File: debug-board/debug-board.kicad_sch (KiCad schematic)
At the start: 31 parts, among them J1 Conn_01x02_Pin, J13 Conn_01x05_Pin, J14 Conn_01x02_Pin, J16 Conn_01x02_Pin, J17 Conn_01x02_Pin, U1 PIC18F47Q84-I/PT, U2 MAX3051ESA+, U3 AZ1117CH-3.3TRG1, Y2 40MHz

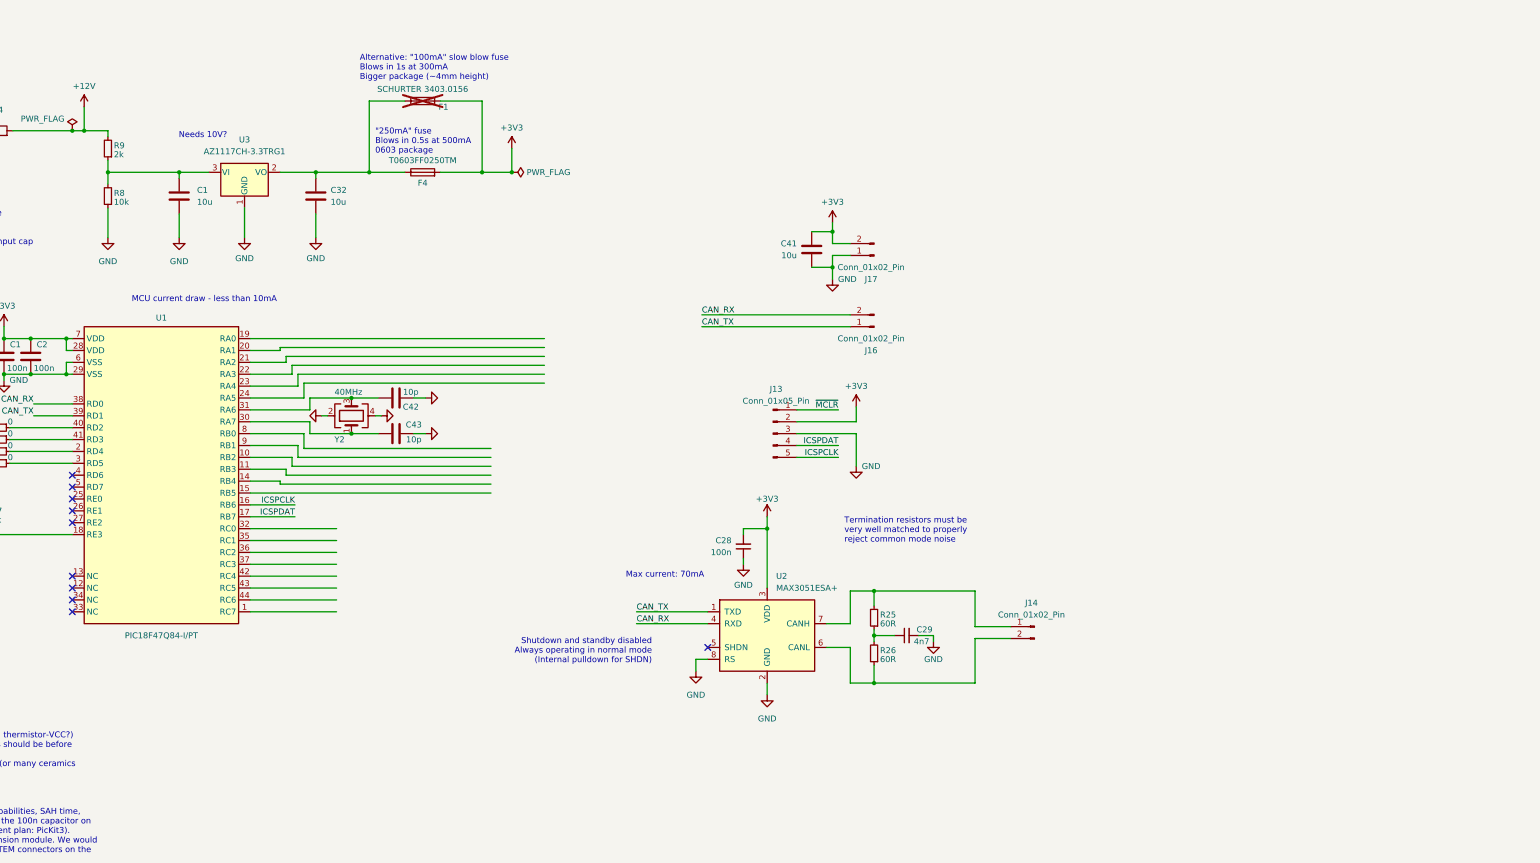
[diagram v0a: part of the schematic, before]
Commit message: Initial design of 12V -> 3V coverter for ADC
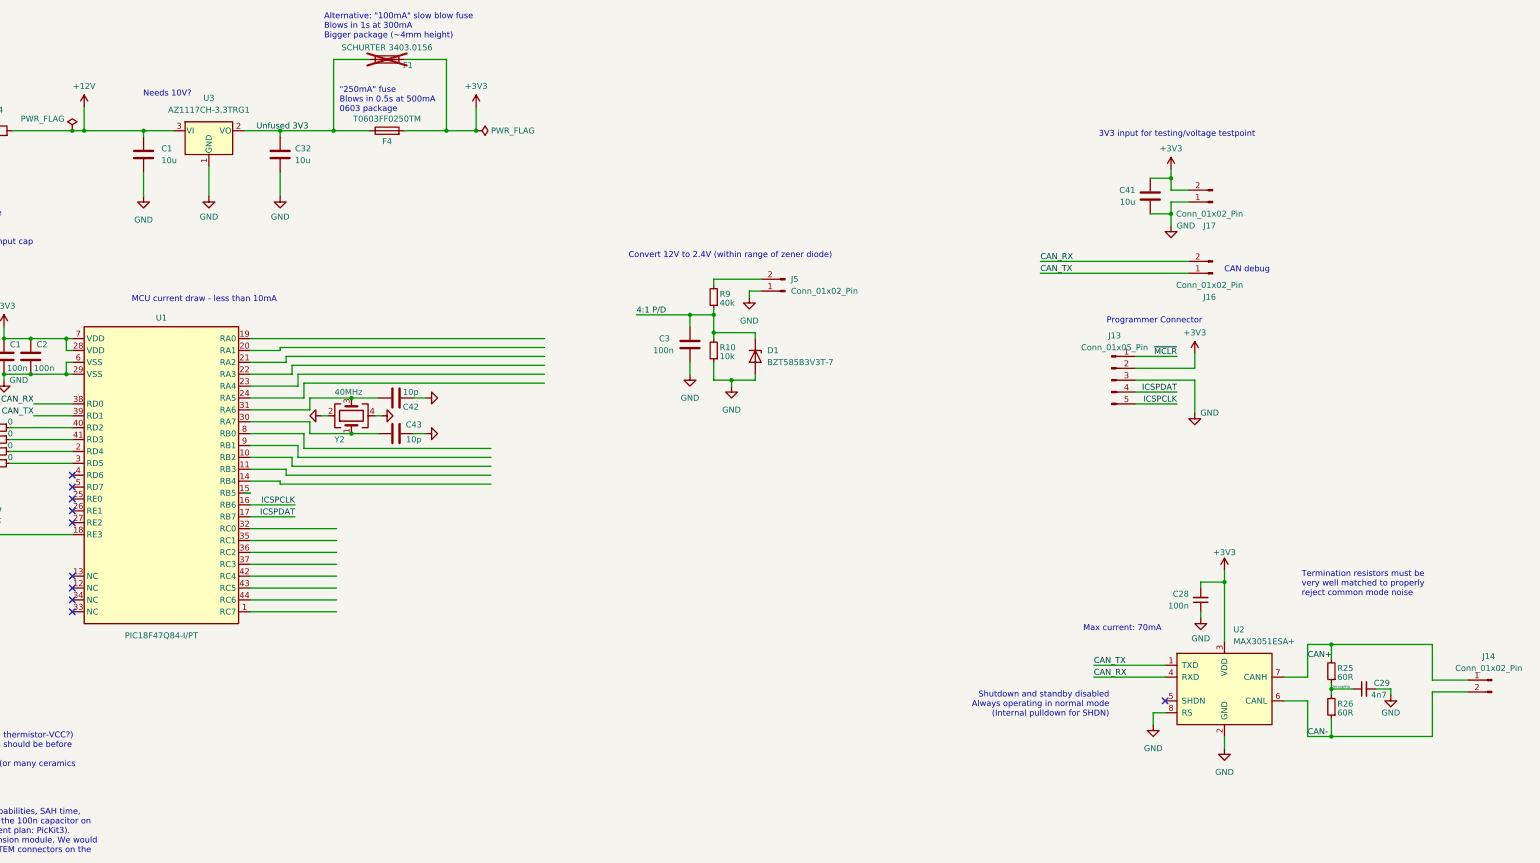
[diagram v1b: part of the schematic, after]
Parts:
- removed R8: 10k, Resistor_SMD:R_0805_2012Metric_Pad1.20x1.40mm_HandSolder, symbol Device:R_Small
- added C3: 100n, Capacitor_SMD:C_0805_2012Metric_Pad1.18x1.45mm_HandSolder, symbol Device:C
- added D1: BZT585B3V3T-7, Diode_SMD:D_SOD-523, symbol Device:D_Zener
- added J5: Conn_01x02_Pin, Connector_Molex:Molex_Micro-Fit_3.0_43650-0200_1x02_P3.00mm_Horizontal, symbol Connector:Conn_01x02_Pin
- added R10: 10k, Resistor_SMD:R_0805_2012Metric_Pad1.20x1.40mm_HandSolder, symbol Device:R_Small
- C1: footprint (none) -> Capacitor_SMD:C_0805_2012Metric_Pad1.18x1.45mm_HandSolder
- F1: now left out of the parts list
- J14: footprint sufst-lib:Conn2_SMD -> Connector_Molex:Molex_Micro-Fit_3.0_43650-0200_1x02_P3.00mm_Horizontal
- R9: value 2k -> 40k; Optional (none) -> True
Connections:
- net +12V: now also C1.1, U3.3 (VI); no longer R9.2
- net GND: now also C3.2, D1.2 (A), J5.1 (Pin_1), R10.1
- net Decoupling: now reaches C29.1, R25.1, R26.2
- net CAN+: now reaches J14.1 (Pin_1), R25.2, U2.7 (CANH)
- net Unfused 3V3: now reaches C32.1, F1.1, F4.1, U3.2 (VO)
- net CAN-: now reaches J14.2 (Pin_2), R26.1, U2.6 (CANL)
- new net: J5.2 (Pin_2), R9.2
- new net 4:1 P/D: C3.1, D1.1 (K), R10.2, R9.1
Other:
- note added: "3V3 input for testing/voltage testpoint"
- note added: "CAN debug"
- note added: "Convert 12V to 2.4V (within range of zener diode)"
- note added: "Programmer Connector"
- company: (none) -> SUFST
- title: (none) -> Debug Board
- moved on the sheet: C1, C28, C29, C32, C41, F1, F4, J13, J14, J16, J17, R25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

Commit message: Add a thermistor sensor and possibly connectors
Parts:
- removed C3: 100n, Capacitor_SMD:C_0805_2012Metric_Pad1.18x1.45mm_HandSolder, symbol Device:C
- added D2: BZT585B3V3T-7, Diode_SMD:D_SOD-523, symbol Device:D_Zener
- added J6, J7: Conn_01x02_Pin, Connector_Molex:Molex_Micro-Fit_3.0_43650-0200_1x02_P3.00mm_Horizontal, symbol Connector:Conn_01x02_Pin
- added R11: 40k, Resistor_SMD:R_0805_2012Metric_Pad1.20x1.40mm_HandSolder, symbol Device:R_Small
- added R12, R13: 10k, Resistor_SMD:R_0805_2012Metric_Pad1.20x1.40mm_HandSolder, symbol Device:R_Small
- J1: footprint (none) -> Connector_Molex:Molex_Micro-Fit_3.0_43650-0200_1x02_P3.00mm_Horizontal
- J13: footprint sufst-lib:Conn5_SMD -> Connector_PinSocket_2.54mm:PinSocket_1x05_P2.54mm_Vertical_SMD_Pin1Left
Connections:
- net +3V3: now also R13.2
- net GND: now also J1.2 (Pin_2), D2.2 (A), J6.1 (Pin_1), J7.1 (Pin_1), R12.1
- net 4:1 P/D renamed 4:1 P/D 1
- new net: J6.2 (Pin_2), R11.2
- new net 4:1 P/D 2: D2.1 (K), R11.1, R12.2
- new net Sensor 1: J7.2 (Pin_2), R13.1
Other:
- note added: "100n cap to gnd on TEM module dont know if needed"
- note added: "Cap is probably not needed (and skews voltages ever so slightly)"
- note added: "Probably not needed/could be a testpoint since we have the programmer connector"
- note added: "Resistors should be measured to maintain ratio"
- note added: "TODO: Replace footprint"
- note added: "Thermistor/Sensor Hookup"
- note removed: "Needs 10V?"
- moved on the sheet: D1, J5, R10, R9

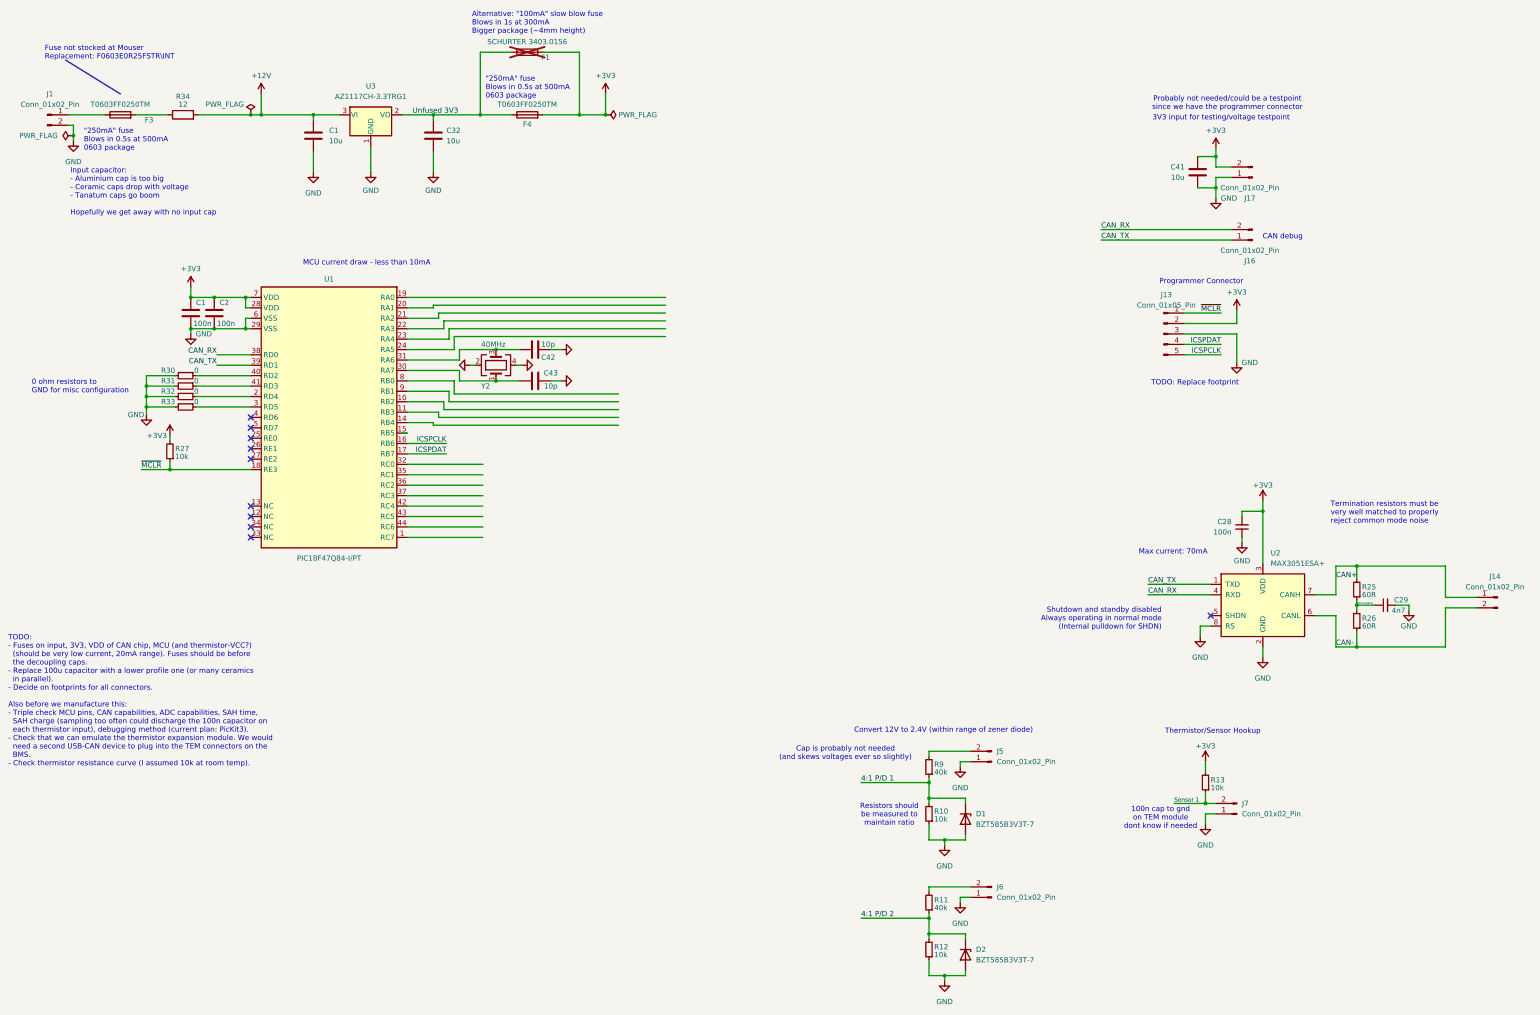
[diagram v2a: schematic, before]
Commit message: Changed footprint need to rearrange things
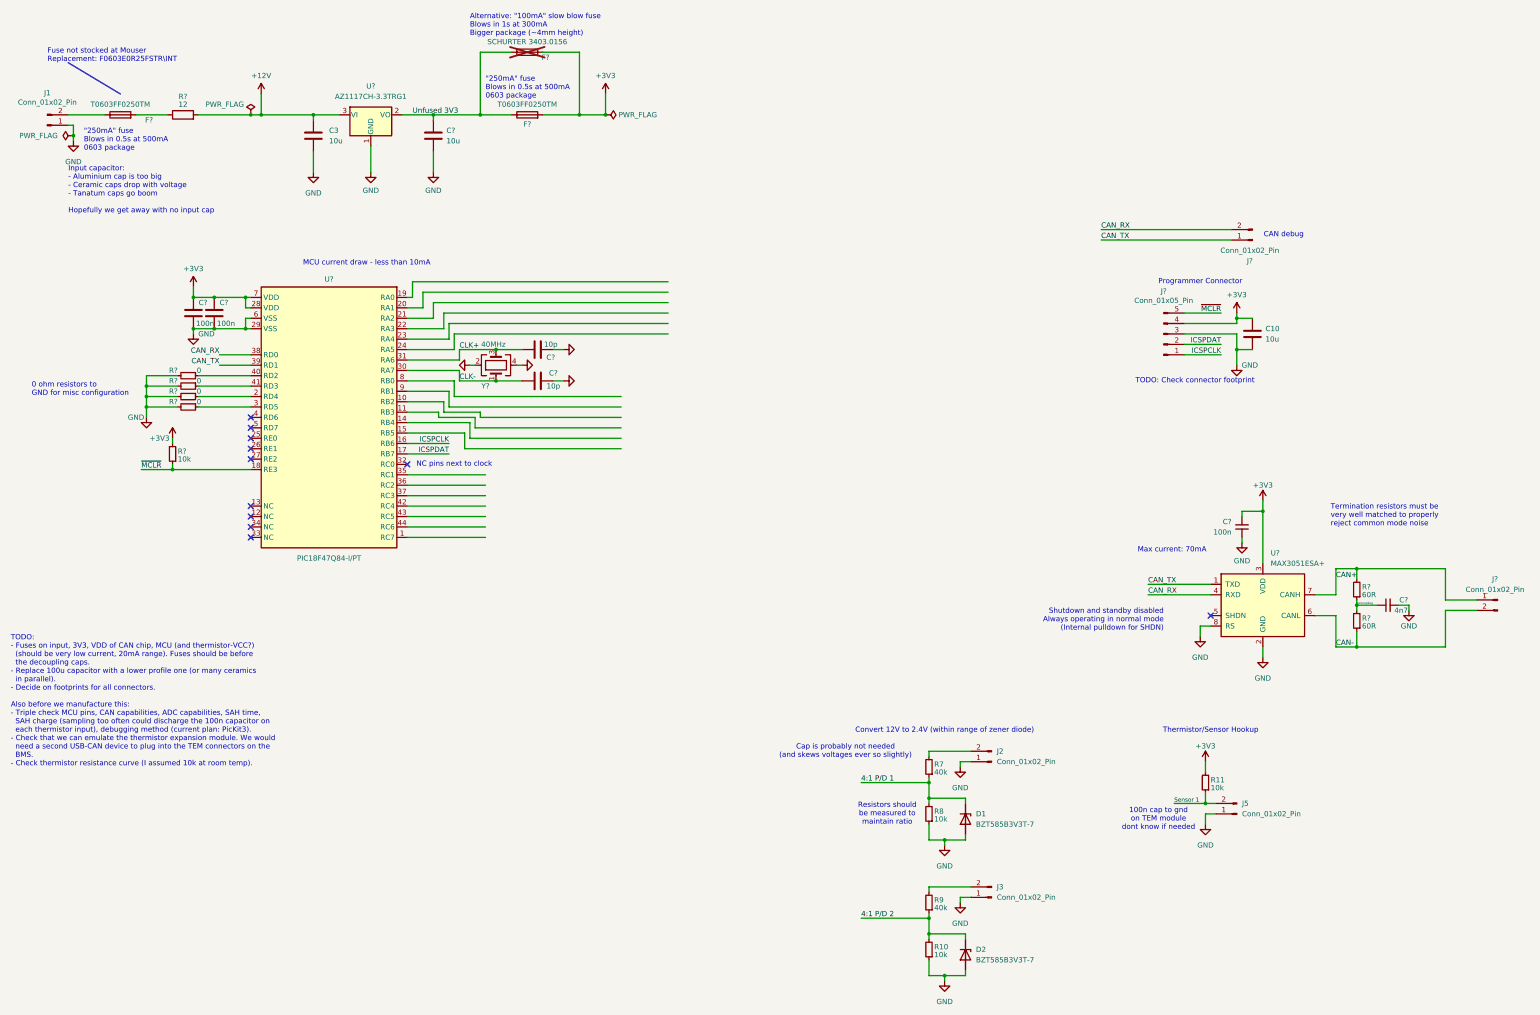
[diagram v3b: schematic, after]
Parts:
- removed C41: 10u, Capacitor_SMD:C_0805_2012Metric_Pad1.18x1.45mm_HandSolder, symbol Device:C
- removed J17: Conn_01x02_Pin, sufst-lib:Conn2_SMD, symbol Connector:Conn_01x02_Pin
- added C10: 10u, Capacitor_SMD:C_0805_2012Metric_Pad1.18x1.45mm_HandSolder, symbol Device:C
- J?: renamed from J13; footprint Connector_PinSocket_2.54mm:PinSocket_1x05_P2.54mm_Vertical_SMD_Pin1Left -> Connector_PinSocket_2.54mm:PinSocket_1x05_P2.54mm_Horizontal
- renumbered C1 to C3, C1 to C?, C42 to C?, C43 to C?, C32 to C?, C29 to C?, C2 to C?, C28 to C?, F3 to F?, F4 to F?, F1 to F?, J5 to J2, J6 to J3, J7 to J5, J16 to J?, J14 to J?, R12 to R10, R13 to R11, R9 to R7, R10 to R8, R11 to R9, R25 to R?, R32 to R?, R34 to R?, R33 to R?, R26 to R?, R30 to R?, R27 to R?, R31 to R?, U3 to U?, U1 to U?, U2 to U?, Y2 to Y?
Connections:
- net +3V3: now also J?.4 (Pin_4), C10.1; no longer J?.2 (Pin_2)
- net GND: now also J1.1 (Pin_1), C10.2; no longer J1.2 (Pin_2)
- net ICSPCLK: now also J?.1 (Pin_1); no longer J?.5 (Pin_5)
- net ICSPDAT: now also J?.2 (Pin_2); no longer J?.4 (Pin_4)
- net ~{MCLR}: now also J?.5 (Pin_5); no longer J?.1 (Pin_1)
- net at F?.1: now also J1.2 (Pin_2); no longer J1.1 (Pin_1)
- net CLK+: now reaches C?.1, U?.31 (RA6), Y?.3
- net CLK-: now reaches C?.1, U?.30 (RA7), Y?.1
- no-connect marks 10 -> 11
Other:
- note added: "NC pins next to clock"
- note added: "TODO: Check connector footprint"
- note removed: "3V3 input for testing/voltage testpoint"
- note removed: "Probably not needed/could be a testpoint since we have the programmer connector"
- note removed: "TODO: Replace footprint"
- moved on the sheet: C?, J?, R?

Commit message: Changed connectors and added another thermistor
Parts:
- added J6: Conn_01x02_Pin, Connector_Molex:Molex_Micro-Fit_3.0_43045-0200_2x01_P3.00mm_Horizontal, symbol Connector:Conn_01x02_Pin
- added R14: 10k, Resistor_SMD:R_0805_2012Metric_Pad1.20x1.40mm_HandSolder, symbol Device:R_Small
- J1, J2, J3, J5, J?: footprint Connector_Molex:Molex_Micro-Fit_3.0_43650-0200_1x02_P3.00mm_Horizontal -> Connector_Molex:Molex_Micro-Fit_3.0_43045-0200_2x01_P3.00mm_Horizontal
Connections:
- net Sensor 1 is gone; now on net Therm 2: J5.2 (Pin_2), R11.1
- net +3V3: now also R14.2
- net 4:1 P/D 1: now also U?.1 (RC7)
- net 4:1 P/D 2: now also U?.44 (RC6)
- net GND: now also J1.2 (Pin_2), J6.1 (Pin_1); no longer J1.1 (Pin_1)
- net at F?.1: now also J1.1 (Pin_1); no longer J1.2 (Pin_2)
- net Therm 2: now reaches U?.8 (RB0)
- net Therm 1: now reaches U?.9 (RB1)
- net Therm 1: now also J6.2 (Pin_2), R14.1
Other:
- moved on the sheet: J1

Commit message: Rearrange board and change connector separation
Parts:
- added D3, D4: BZT585B3V3T-7, Diode_SMD:D_SOD-523, symbol Device:D_Zener
- added J10, J9: Conn_01x02_Pin, Connector_Molex:Molex_Micro-Fit_3.0_43045-0200_2x01_P3.00mm_Horizontal, symbol Connector:Conn_01x02_Pin
- added R15, R17: 40k, Resistor_SMD:R_0805_2012Metric_Pad1.20x1.40mm_HandSolder, symbol Device:R_Small
- added R16, R18: 10k, Resistor_SMD:R_0805_2012Metric_Pad1.20x1.40mm_HandSolder, symbol Device:R_Small
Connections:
- net 4:1 P/D 1: now also U?.36 (RC2); no longer U?.1 (RC7)
- net 4:1 P/D 2: now also U?.35 (RC1); no longer U?.44 (RC6)
- net CAN+: now also J?.2 (Pin_2); no longer J?.1 (Pin_1)
- net CAN-: now also J?.1 (Pin_1); no longer J?.2 (Pin_2)
- net GND: now also D3.2 (A), D4.2 (A), J10.1 (Pin_1), J9.1 (Pin_1), R16.1, R18.1
- net Therm 1: now also U?.23 (RA4); no longer U?.9 (RB1)
- net Therm 2: now also U?.22 (RA3); no longer U?.8 (RB0)
- net 4:1 P/D 3: now reaches U?.37 (RC3)
- net 4:1 P/D 3: now also D3.1 (K), R15.1, R16.2
- net 4:1 P/D 4: now reaches U?.42 (RC4)
- net 4:1 P/D 4: now also D4.1 (K), R17.1, R18.2
- new net: J10.2 (Pin_2), R17.2
- new net: J9.2 (Pin_2), R15.2
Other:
- moved on the sheet: C10, C?, D1, D2, J2, J3, J5, J6, J?, R10, R11, R14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
